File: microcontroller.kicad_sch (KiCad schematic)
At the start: 40 parts, among them J4 Conn_01x02, J5 SWD, SW1 SW_SPDT, U2 STM32F105RCTx, U3 SN65HVD230, U4 CD143A-SR05, Y1 16MHz

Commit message: Redo of placement
Really like this attempt
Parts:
- C10, C11, C12, C13, C14, C3, C4, C5, C6, C7, C8, C9: footprint Capacitor_SMD:C_0603_1608Metric -> Capacitor_SMD:C_0603_1608Metric_Pad1.08x0.95mm_HandSolder
- D1: footprint LED_SMD:LED_0603_1608Metric -> LED_SMD:LED_0603_1608Metric_Pad1.05x0.95mm_HandSolder
- R10, R11, R12, R13, R14, R2, R3, R4, R5, R6, R7, R8, R9: footprint Resistor_SMD:R_0603_1608Metric -> Resistor_SMD:R_0603_1608Metric_Pad0.98x0.95mm_HandSolder
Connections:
- net DIFF+: now reaches C11.1, JP1.1 (A), R10.1, R12.1, TP3.1, U3.7 (CANH)
- net DIFF+: now also U4.2 (I/O_1); no longer U4.3 (I/O_2)
- net DIFF-: now reaches C10.1, JP2.1 (A), R8.2, R9.2, TP4.1, U3.6 (CANL)
- net DIFF-: now also U4.3 (I/O_2); no longer U4.2 (I/O_1)

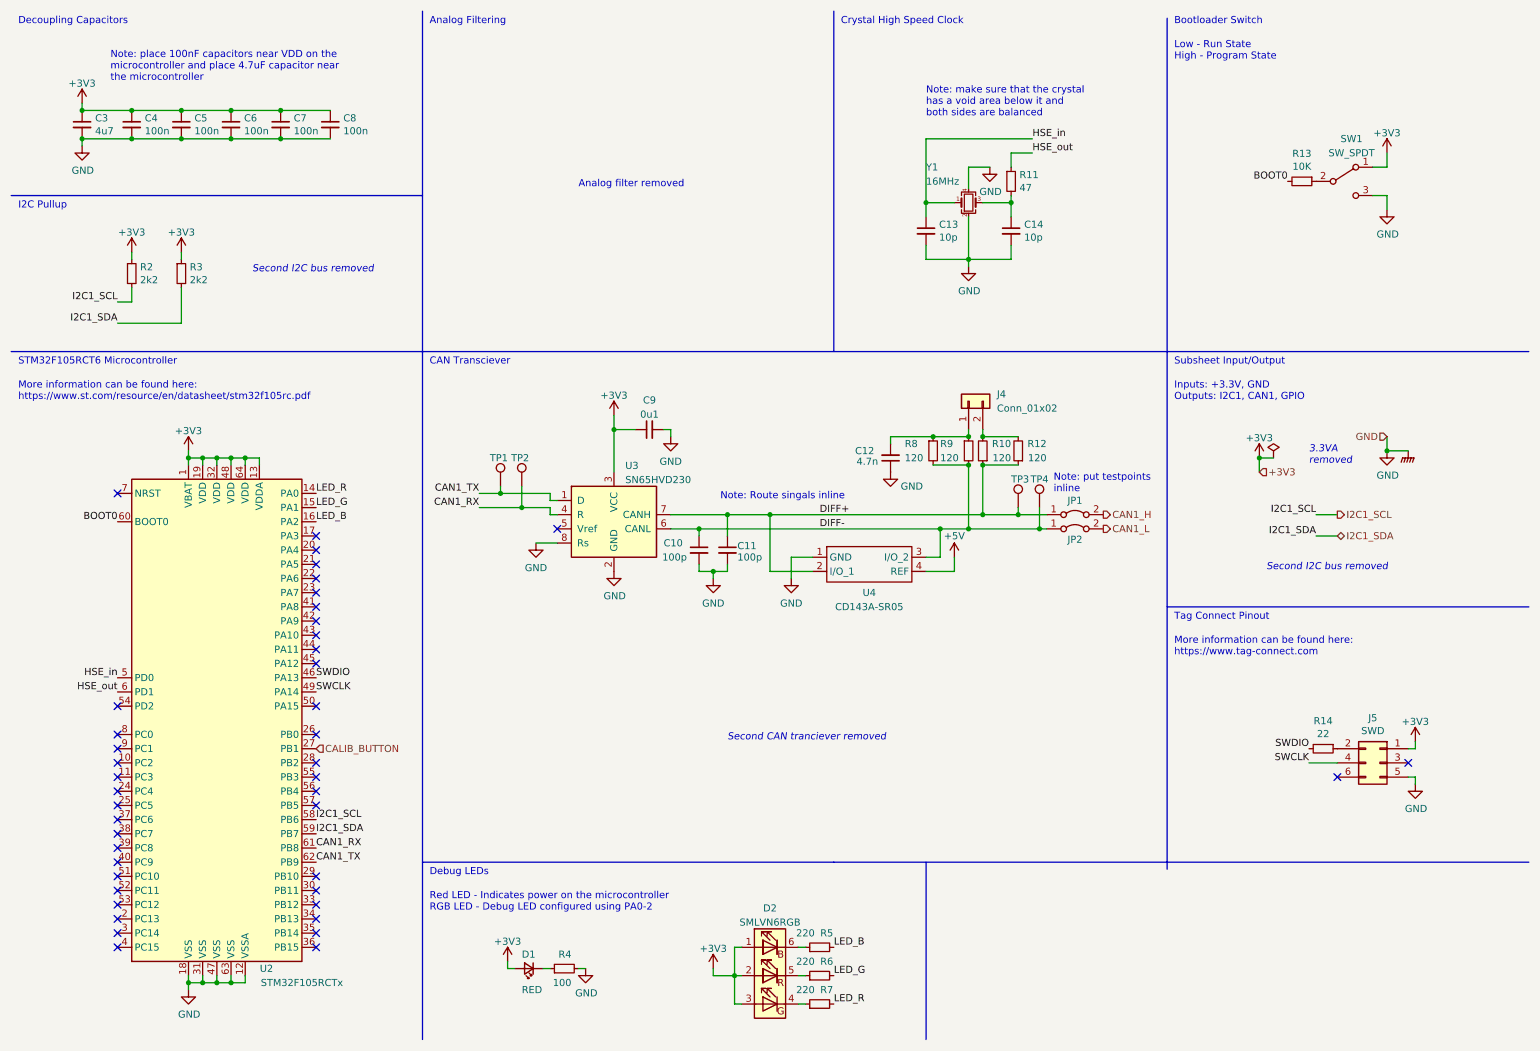
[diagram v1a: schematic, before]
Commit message: Added 0 Ohm resistor between shield (grounded)
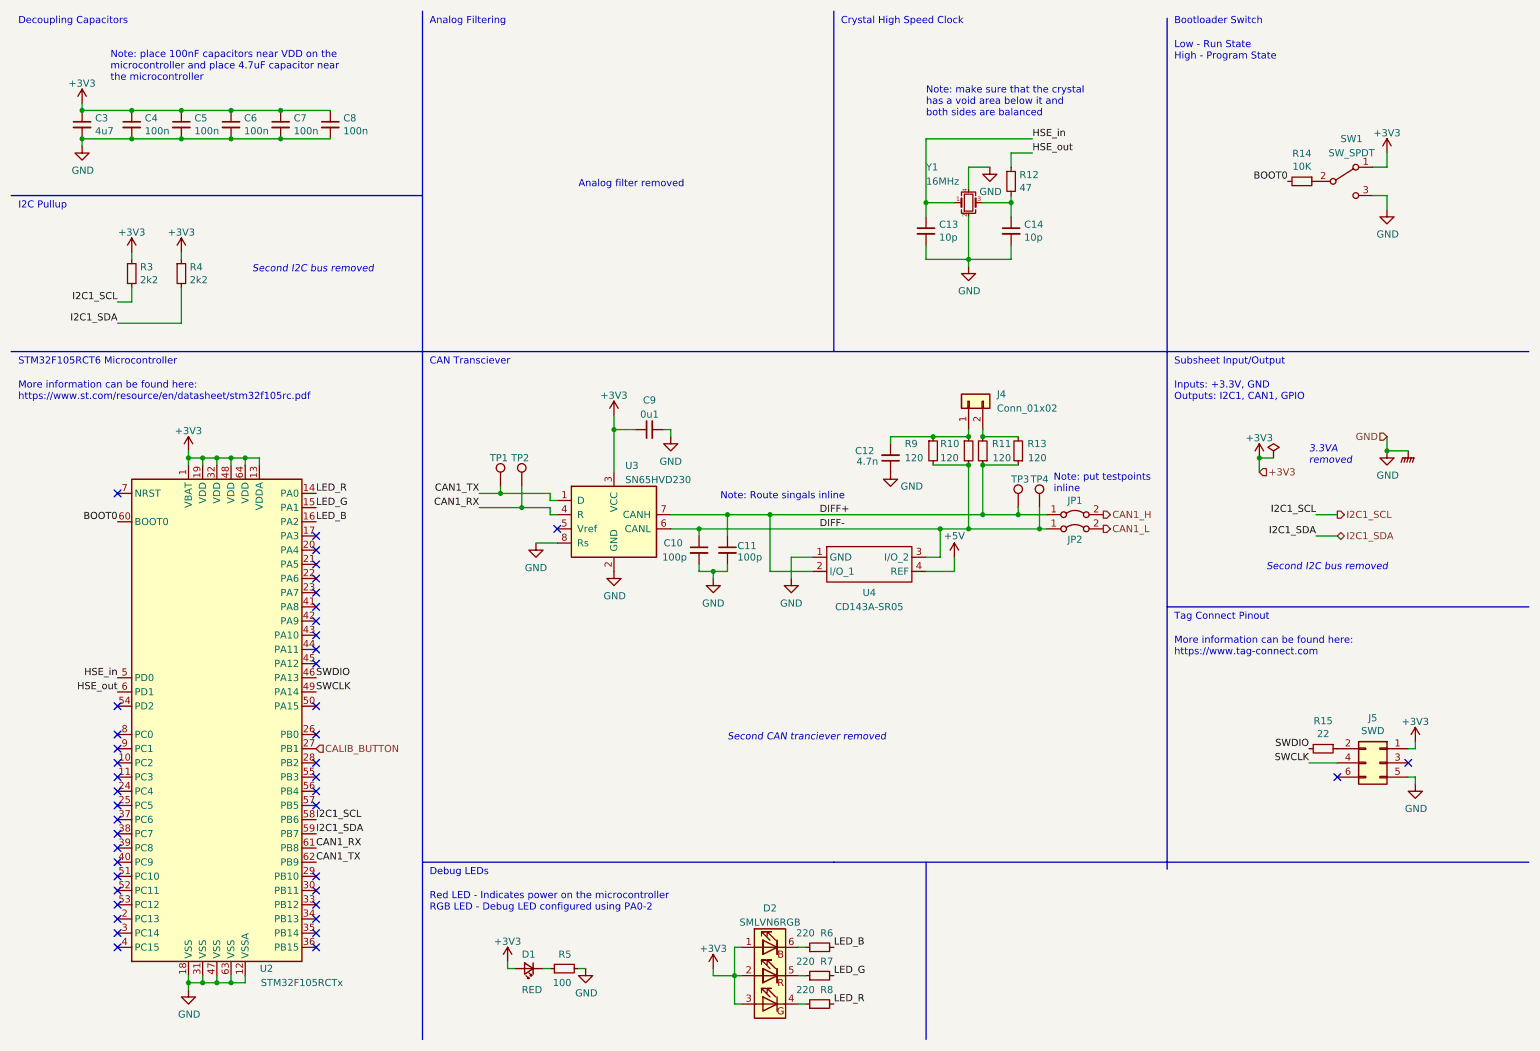
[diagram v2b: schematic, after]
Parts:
- renumbered R9 to R10, R10 to R11, R11 to R12, R12 to R13, R13 to R14, R14 to R15, R2 to R3, R3 to R4, R4 to R5, R5 to R6, R6 to R7, R7 to R8, R8 to R9
